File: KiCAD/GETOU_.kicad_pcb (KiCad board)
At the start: 2 copper layers, 116 x 60 mm, 25 parts, among them U1 XIAO-RP2040-DIP

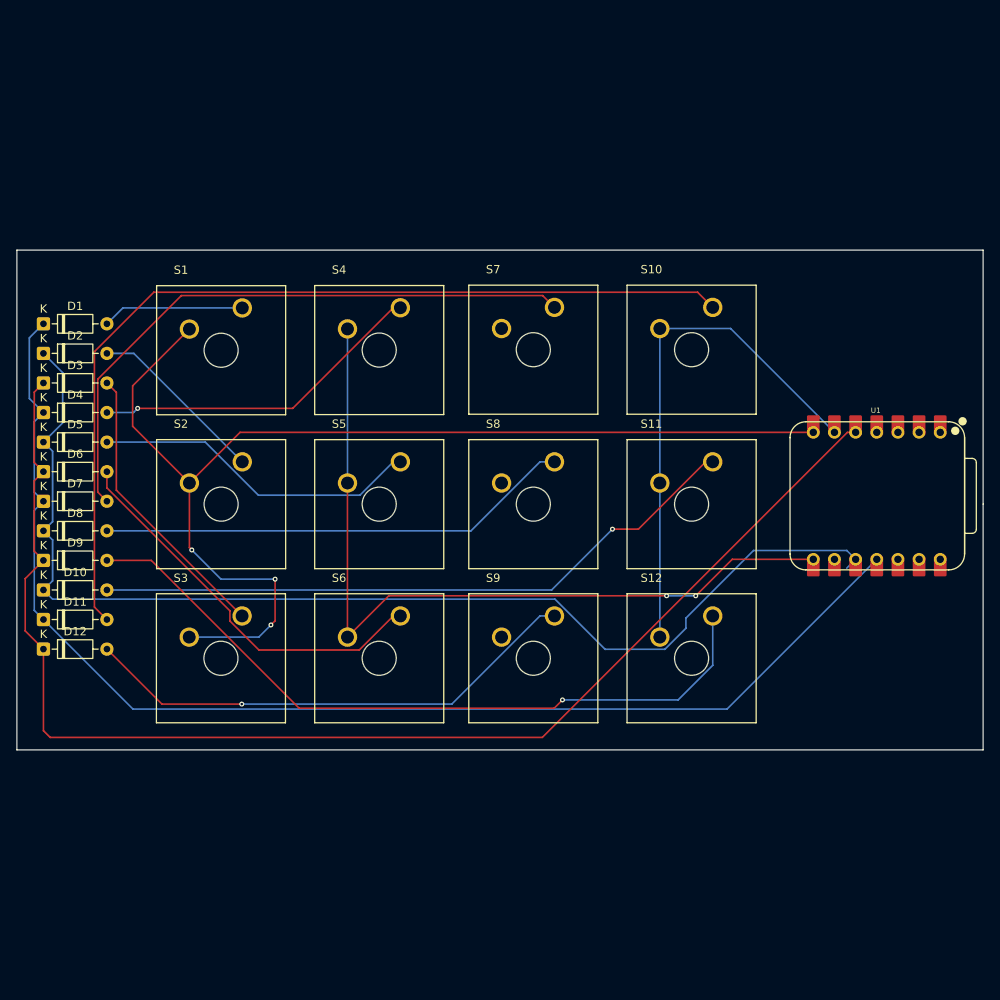
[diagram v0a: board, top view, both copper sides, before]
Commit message: Delete getoucompanion and redo qmk firmware
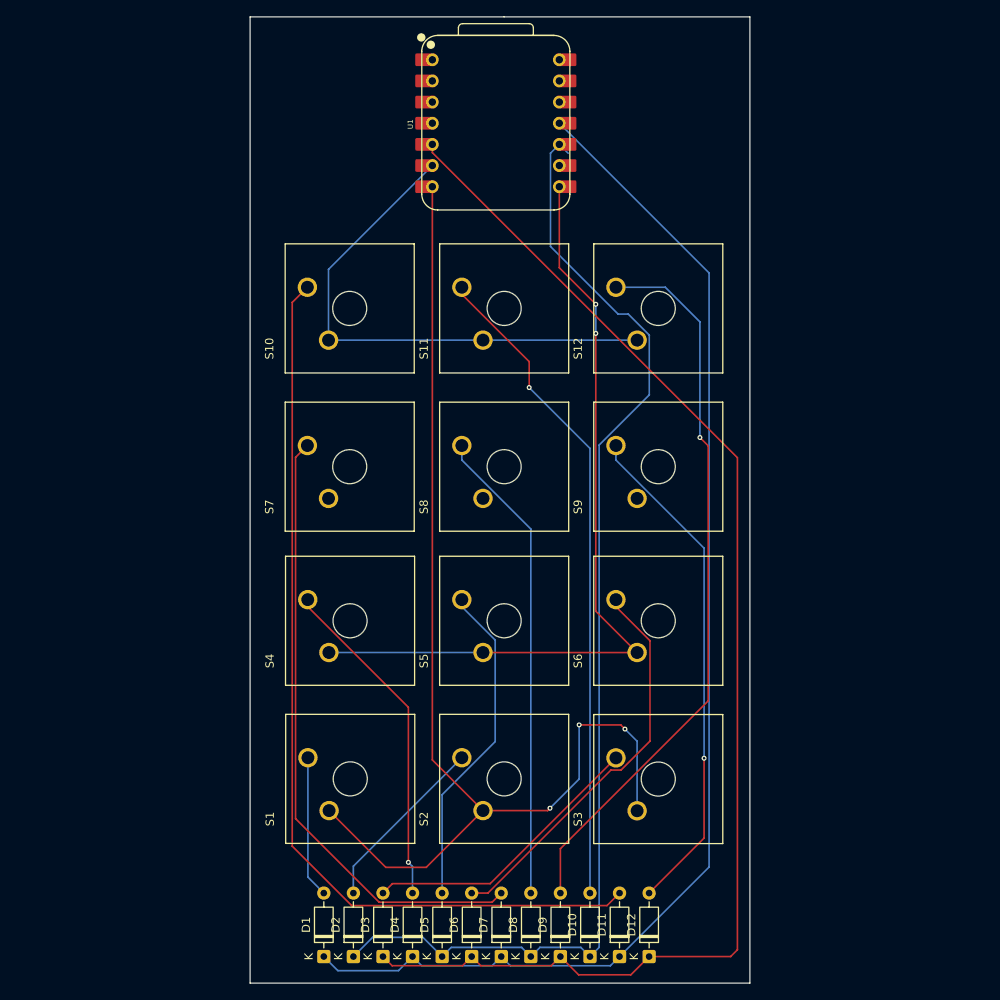
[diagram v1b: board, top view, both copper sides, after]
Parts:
- moved D1 83.1 mm to (104.8, 149.8), turned to 90 degrees
- moved D12 81.5 mm to (143.9, 149.8), turned to 90 degrees
- moved D2 81.4 mm to (108.4, 149.8), turned to 90 degrees
- moved D11 80.1 mm to (140.3, 149.8), turned to 90 degrees
- moved D3 80.0 mm to (112.0, 149.8), turned to 90 degrees
- moved D10 79.0 mm to (136.8, 149.8), turned to 90 degrees
- moved D4 78.9 mm to (115.5, 149.8), turned to 90 degrees
- moved D9 78.2 mm to (133.2, 149.8), turned to 90 degrees
- moved D5 78.1 mm to (119.0, 149.8), turned to 90 degrees
- moved D8 77.7 mm to (129.7, 149.8), turned to 90 degrees
- moved D6 77.7 mm to (122.6, 149.8), turned to 90 degrees
- moved D7 77.5 mm to (126.2, 149.8), turned to 90 degrees
- moved U1 64.0 mm to (125.5, 49.8), turned to 90 degrees
- moved S3 54.5 mm to (145.0, 128.5), turned to 90 degrees
- moved S1 53.7 mm to (108.0, 128.5), turned to 90 degrees
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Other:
- board size 116 x 60 mm -> 60 x 116 mm
